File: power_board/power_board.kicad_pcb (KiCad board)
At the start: 4 copper layers, 100 x 100 mm, 158 parts, among them CN1 XT90PW-M.G.Y, CN2 XT60PW-M, J1 Conn_ARM_SWD_TagConnect_TC203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, Q1 BSC0702LS, Q2 BSC0702LS, Q3 BSC0702LS, Q4 BSC0702LS, Q5 BSC0702LS, Q6 BSC0702LS, U1 MR60PW-M.G.B, U10 66565S0M3, U11 LM5163DDAR, U12 LP2985-33DBVR, U13 LP2985-33DBVR, U14 LP2985-33DBVR, U15 CONTROL, U16 SWD, U2 LM66100DCKR, U3 STM32L431KCUx, U4 INA180A1, U5 UCC27282DRCR, U6 66565S0M3, U7 UCC27282DRCR, U8 66565S0M3, U9 UCC27282DRCR

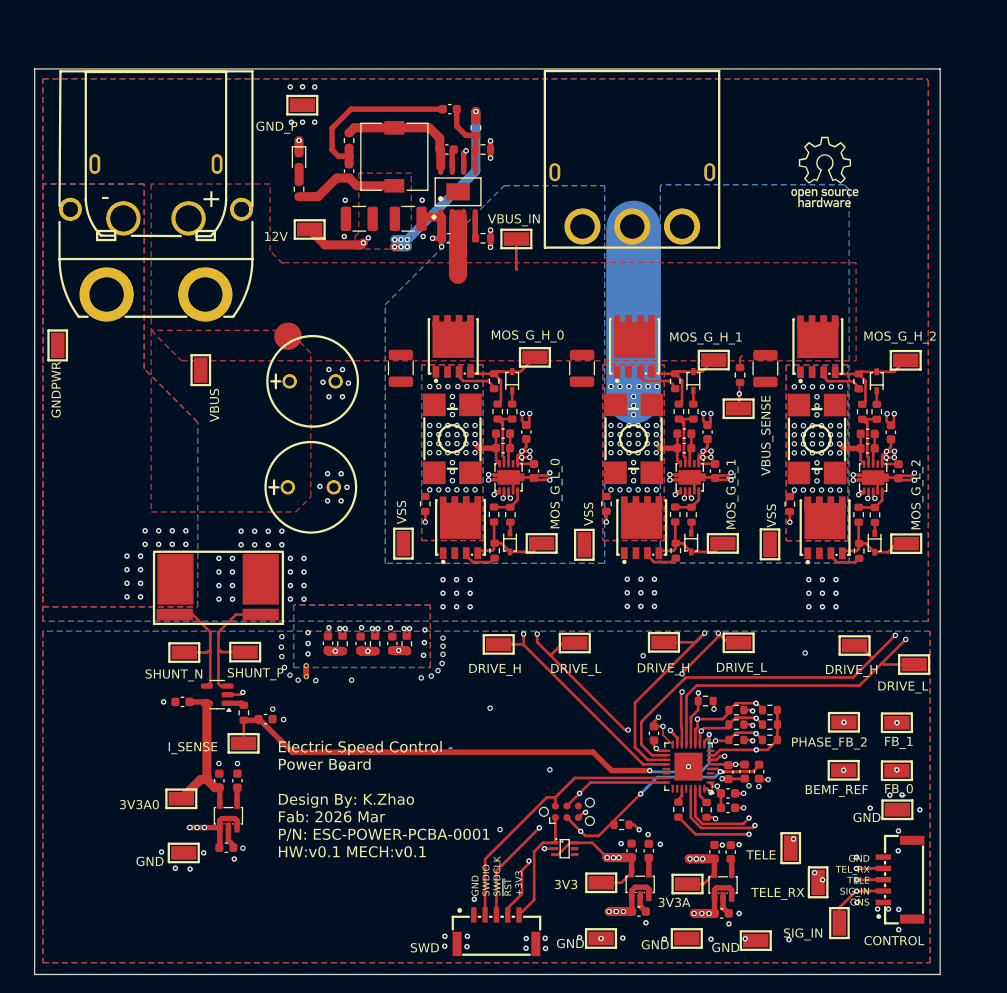
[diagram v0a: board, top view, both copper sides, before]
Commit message: change mcu to STM32F051K8U6
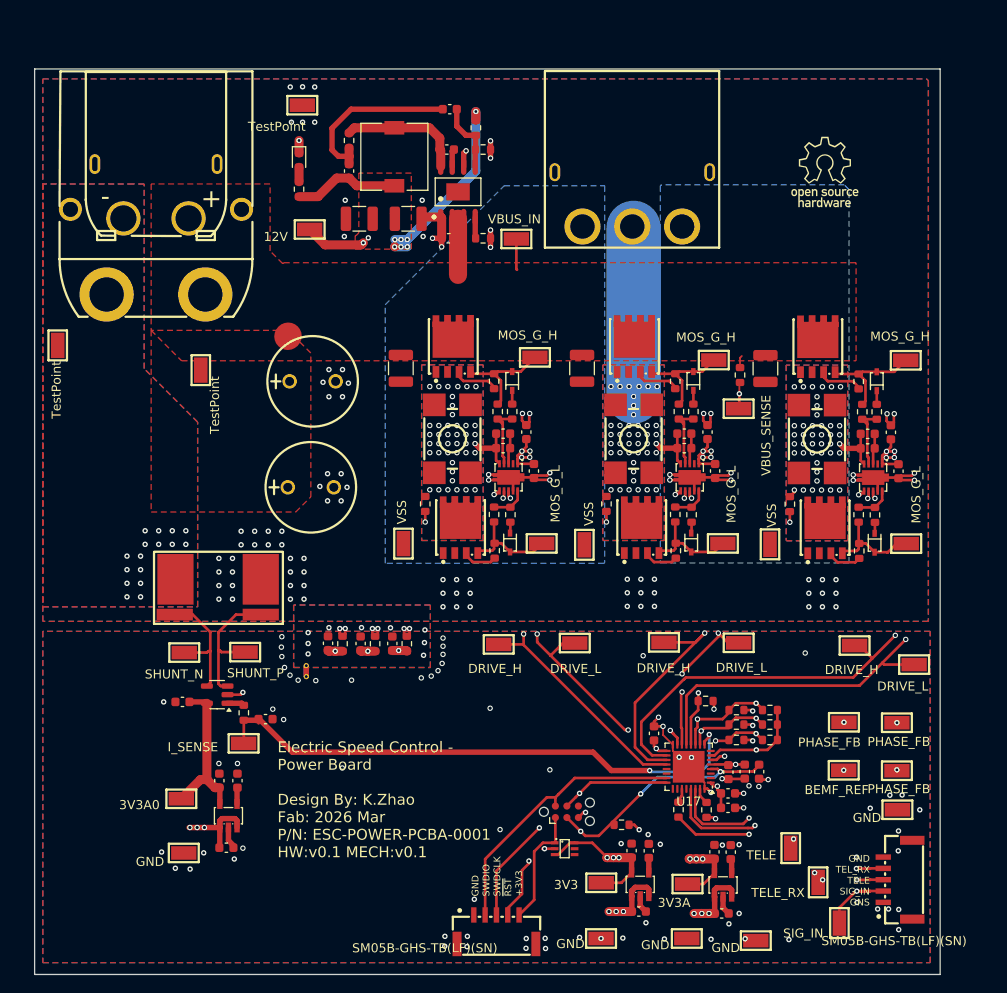
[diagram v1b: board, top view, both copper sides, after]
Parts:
- removed U3: STM32L431KCUx, Package_DFN_QFN:QFN-32-1EP_5x5mm_P0.5mm_EP3.1x3.1mm
- added U17: STM32F051K8Tx, Package_DFN_QFN:UFQFPN-32-1EP_5x5mm_P0.5mm_EP3.5x3.5mm, F.Cu at (92.1, 96.8)
- L1: value L_Small -> 100u
- TP10: value MOS_G_H_0 -> MOS_G_H
- TP13: value FB_0 -> PHASE_FB
- TP14: value MOS_G_L_1 -> MOS_G_L
- TP15: value MOS_G_H_1 -> MOS_G_H
- TP18: value FB_1 -> PHASE_FB
- TP19: value MOS_G_L_2 -> MOS_G_L
- TP20: value MOS_G_H_2 -> MOS_G_H
- TP23: value PHASE_FB_2 -> PHASE_FB
- TP30: value VBUS -> TestPoint
- TP31: value GNDPWR -> TestPoint
- TP34: value GND_P -> TestPoint
- TP9: value MOS_G_L_0 -> MOS_G_L
- U15: value CONTROL -> SM05B-GHS-TB(LF)(SN)
- U16: value SWD -> SM05B-GHS-TB(LF)(SN)
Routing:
- net GND: track 26.3 -> 33.6 mm, vias 86 -> 87

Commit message: Add JLCJLCJLCJLC
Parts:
- added H1: MountingHole_Pad, MountingHole:MountingHole_4.3mm_M4_Pad_Via, F.Cu at (28.0, 104.0)
- added H2: MountingHole_Pad, MountingHole:MountingHole_4.3mm_M4_Pad_Via, F.Cu at (108.0, 24.0)
- TP30: value TestPoint -> VBUS
- TP31: value TestPoint -> PWRGND
- TP34: value TestPoint -> PGND
- moved C22 5.87 mm to (112.7, 54.2)
- moved C23 5.87 mm to (110.1, 54.4)
- moved C24 5.87 mm to (110.1, 56.0)
- moved C29 5.87 mm to (94.0, 107.4)
- moved C33 5.87 mm to (95.0, 100.6)
- moved C4 5.87 mm to (94.7, 91.8)
- moved D1 5.87 mm to (70.6, 66.4)
- moved D6 5.87 mm to (111.1, 48.6)
- moved J1 5.87 mm to (76.9, 96.1)
- moved R18 5.87 mm to (95.6, 88.2)
- moved R28 5.87 mm to (111.1, 52.0)
- moved R31 5.87 mm to (109.2, 67.3)
- moved R32 5.87 mm to (109.1, 48.6)
- moved R34 5.87 mm to (95.6, 84.9)
- moved TP11 5.87 mm to (69.3, 77.7)
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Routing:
- net GND: vias 87 -> 86
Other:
- board text added: "JLCJLCJLCJLC"
